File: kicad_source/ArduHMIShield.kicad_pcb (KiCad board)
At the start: 2 copper layers, 72 x 53 mm, 52 parts, among them CN1 ARDUINO_ISP, CN2 ARDUINO_MKR, Q1 2N7002, SW1 TAST_VER, SW2 TAST_VER, SW3 TAST_VER, SW4 TAST_VER, SW5 TAST_VER, SW6 TAST_VER, U1 LT1117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

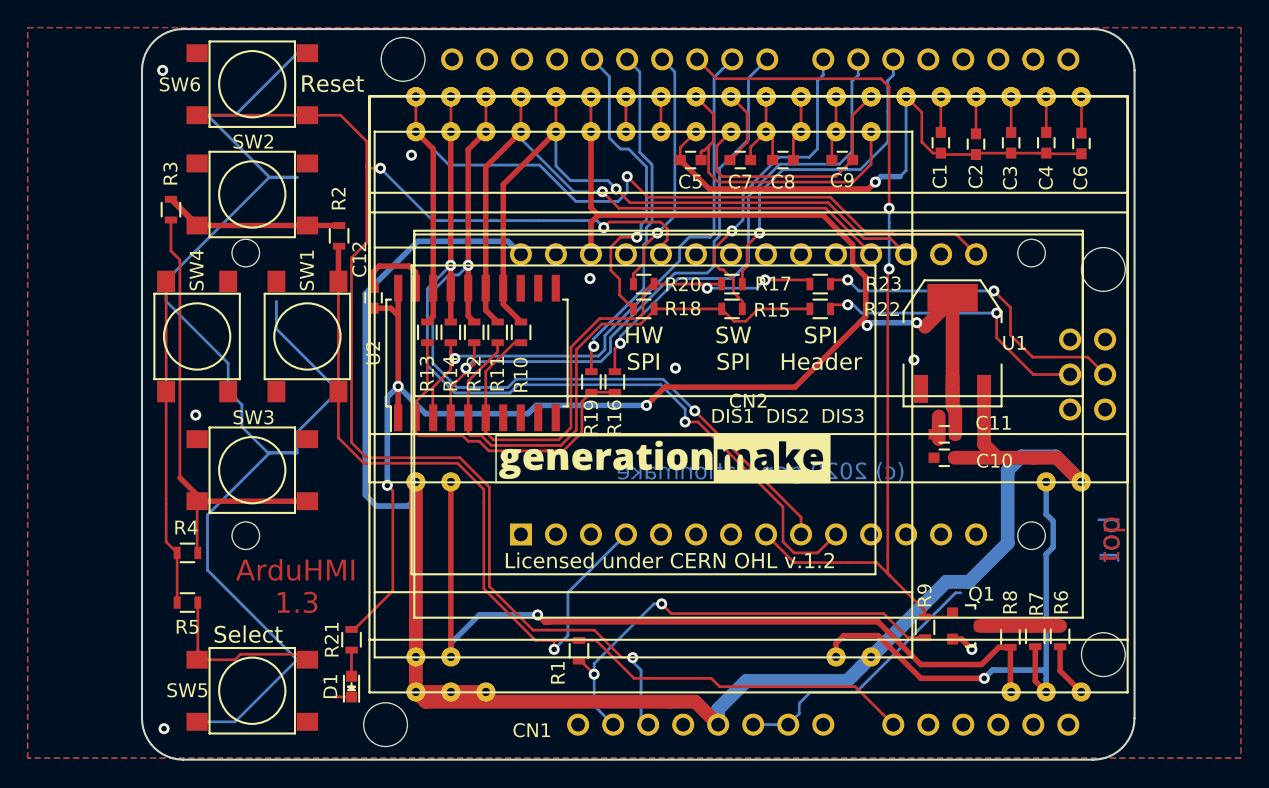
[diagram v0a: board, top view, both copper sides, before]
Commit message: updated order numbers
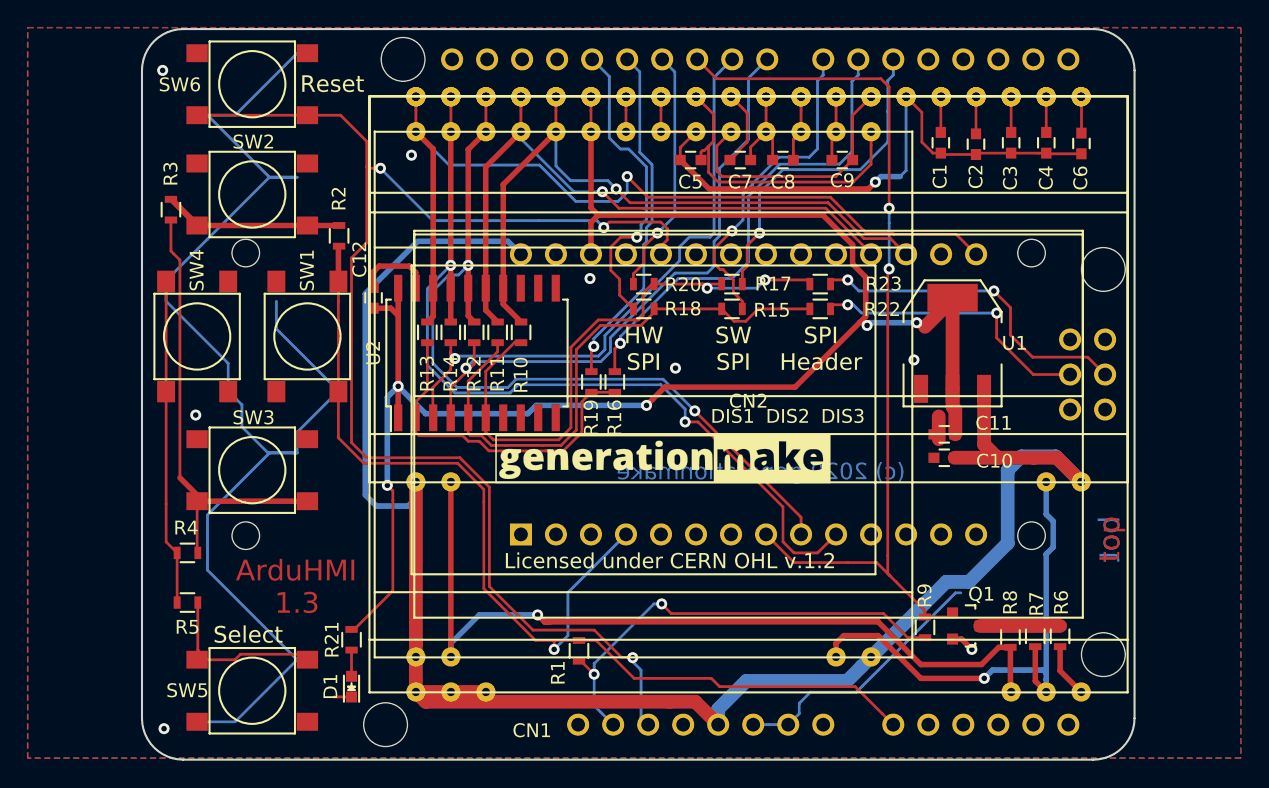
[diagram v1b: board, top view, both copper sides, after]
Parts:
- D1: value green -> 150060GS75000
- U1: value LT1117 -> AZ1117IH-3.3
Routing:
- net (no net): track 5.07 -> 0.00 mm

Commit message: generated pdfs, updated changes file
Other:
- board text added: "Copyright generationmake 2020 see full project documentation at https://github.com/generationmake/ArduHMIShield This documentation describes Open Hardware and is licensed under the CERN OHL v. 1.2. You may redistribute and modify this documentation under the terms of the CERN OHL v.1.2. (http://ohwr.org/cernohl). This documentation is distributed WITHOUT ANY EXPRESS OR IMPLIED WARRANTY, INCLUDING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"
- board text removed: "Copyright generationmake 2019 see full project documentation at http://arduhmi.generationmake.de This documentation describes Open Hardware and is licensed under the CERN OHL v. 1.2. You may redistribute and modify this documentation under the terms of the CERN OHL v.1.2. (http://ohwr.org/cernohl). This documentation is distributed WITHOUT ANY EXPRESS OR IMPLIED WARRANTY, INCLUDING OF MERCHANTABI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"
